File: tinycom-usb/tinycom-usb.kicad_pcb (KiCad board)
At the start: 2 copper layers, 45.2 x 45.2 mm, 65 parts, among them J1 MICRO_SD_HINGE, P1 CONN_02X10, P2 CONN_02X10, P3 USB_A, P4 USB_OTG, U1 SY8008BAAC, U2 AXP209, U3 SY8008BAAC, U4 RTL8188, U5 rainsun-antenna

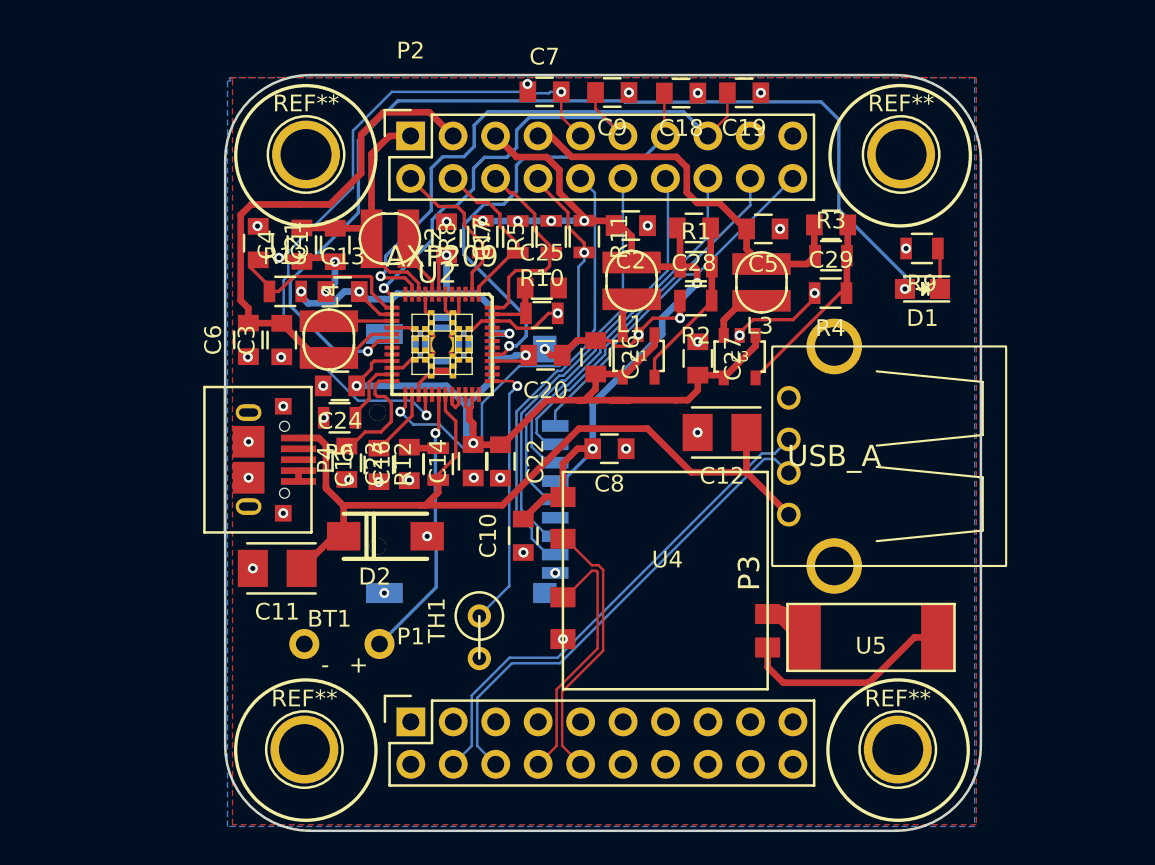
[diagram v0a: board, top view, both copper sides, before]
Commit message: improve tinycom-usb (usb connector+antenna)
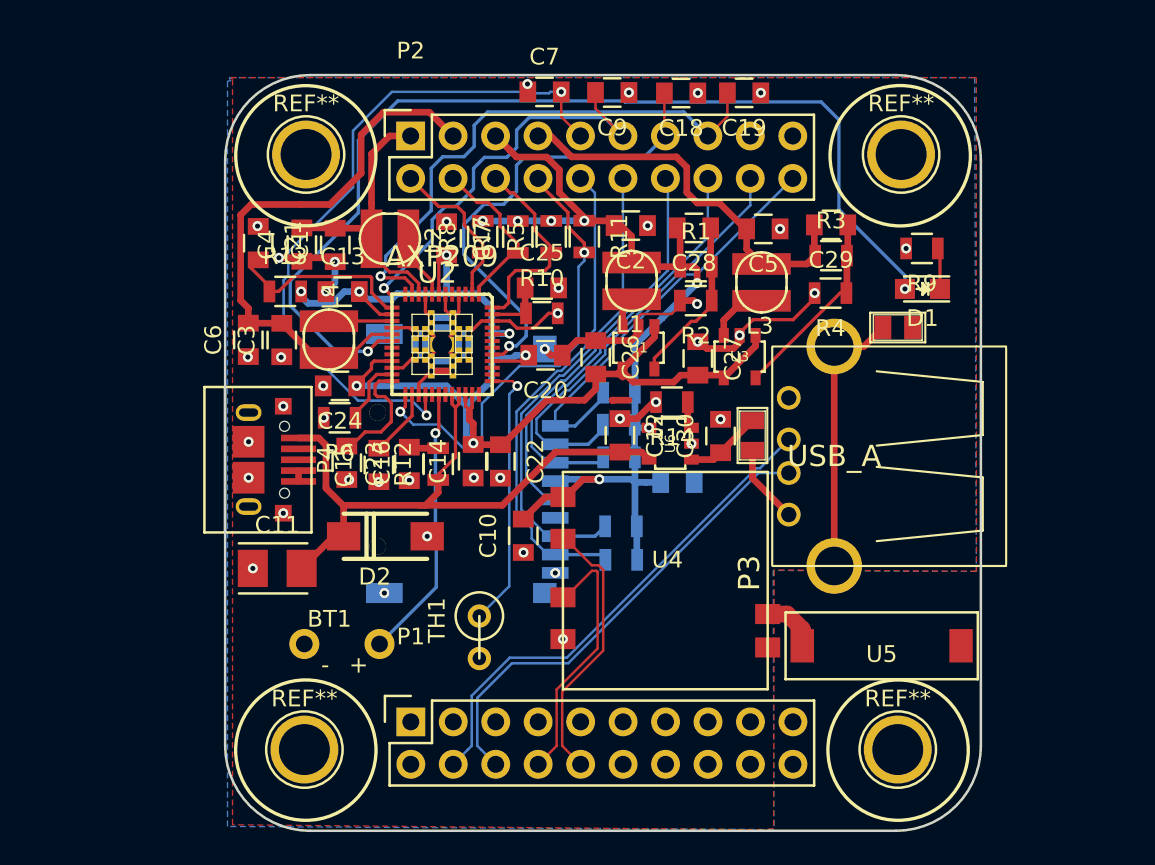
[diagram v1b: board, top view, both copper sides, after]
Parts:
- added C30: 10uF, Capacitors_SMD:C_0805, F.Cu at (154.1, 100.8)
- added L5: SMD-FERRITE-BEAD-200R-2A(0805), OPL-Inductor-L0805, F.Cu at (164.7, 94.4)
- added L6: SMD-FERRITE-BEAD-200R-2A(0805), OPL-Inductor-L0805, F.Cu at (156.0, 100.8)
- added R14: 6.8K, Resistors_SMD:R_0805, F.Cu at (151.2, 98.8)
- added R15: 100K, Resistors_SMD:R_0805, B.Cu at (148.0, 98.3)
- added R16: 100K, Resistors_SMD:R_0805, B.Cu at (148.0, 100.2)
- added R17: 100K, Resistors_SMD:R_0805, B.Cu at (148.0, 102.1)
- added R19: 100K, Resistors_SMD:R_0805, B.Cu at (148.1, 106.2)
- added R20: 100K, Resistors_SMD:R_0805, B.Cu at (148.2, 108.3)
- added U6: SY6280AAC(SOT23-5), opendous:SOT23-5_Opendous, F.Cu at (151.1, 101.3)
- C11: value CP_Small -> 10uF
- C12: value CP_Small -> 10uF; footprint Capacitors_Tantalum_SMD:TantalC_SizeB_EIA-3528_Reflow -> Capacitors_SMD:C_0805
- C8: moved to B.Cu
- U5: footprint tinycom:rainsun-antenna -> tinycom:AN9520
- moved C12 6.11 mm to (148.1, 100.8), turned to 270 degrees
- moved C8 4.54 mm to (151.5, 103.6)
- moved U5 0.81 mm to (163.7, 113.4)
- moved U1 0.49 mm to (149.2, 95.6)
- turned C11 to 0 degrees
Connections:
- C11 pad 1: +5V -> GND
- C11 pad 2: GND -> +5V
- C12 pad 1: +5V -> GND
- C12 pad 2: GND -> +5V
- P3 pad 1: +5V -> USB_5V
- P3 pad 5: GND -> Net-(L5-Pad2)
- U2 pad 31: +5V -> Net-(U2-Pad31)
- U2 pad 32: Net-(U2-Pad32) -> +5V
- U2 pad 33: Net-(U2-Pad32) -> +5V
- U4 pad 5: Net-(U4-Pad5) -> GND
- U5 pad 2: Net-(U4-Pad5) -> Net-(U5-Pad2)
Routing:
- net Net-(L5-Pad2): track 0.00 -> 16.5 mm
- net Net-(U4-Pad5): track 12.9 -> 0.00 mm
- net +5V: track 51.9 -> 39.1 mm
- net VCC_33: track 50.0 -> 58.5 mm, vias 6 -> 7
- net GND: track 63.9 -> 70.5 mm, vias 40 -> 42
- net USB_5V: track 0.00 -> 4.74 mm
- net Net-(C30-Pad1): track 0.00 -> 4.63 mm
- net IPSOUT: track 80.7 -> 76.7 mm
- net SDC0_D2: track 21.1 -> 25.0 mm
- net SDC0_D3: track 22.2 -> 25.7 mm
- net SDC0_D0: track 25.2 -> 28.4 mm
- net SDC0_D1: track 26.2 -> 29.3 mm
- net SDC0_CMD: track 22.4 -> 25.4 mm
- net Net-(U2-Pad32): track 1.71 -> 0.00 mm
- net Net-(R14-Pad1): track 0.00 -> 1.63 mm
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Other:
- net class Default: trace_width 0.4 -> 0.15

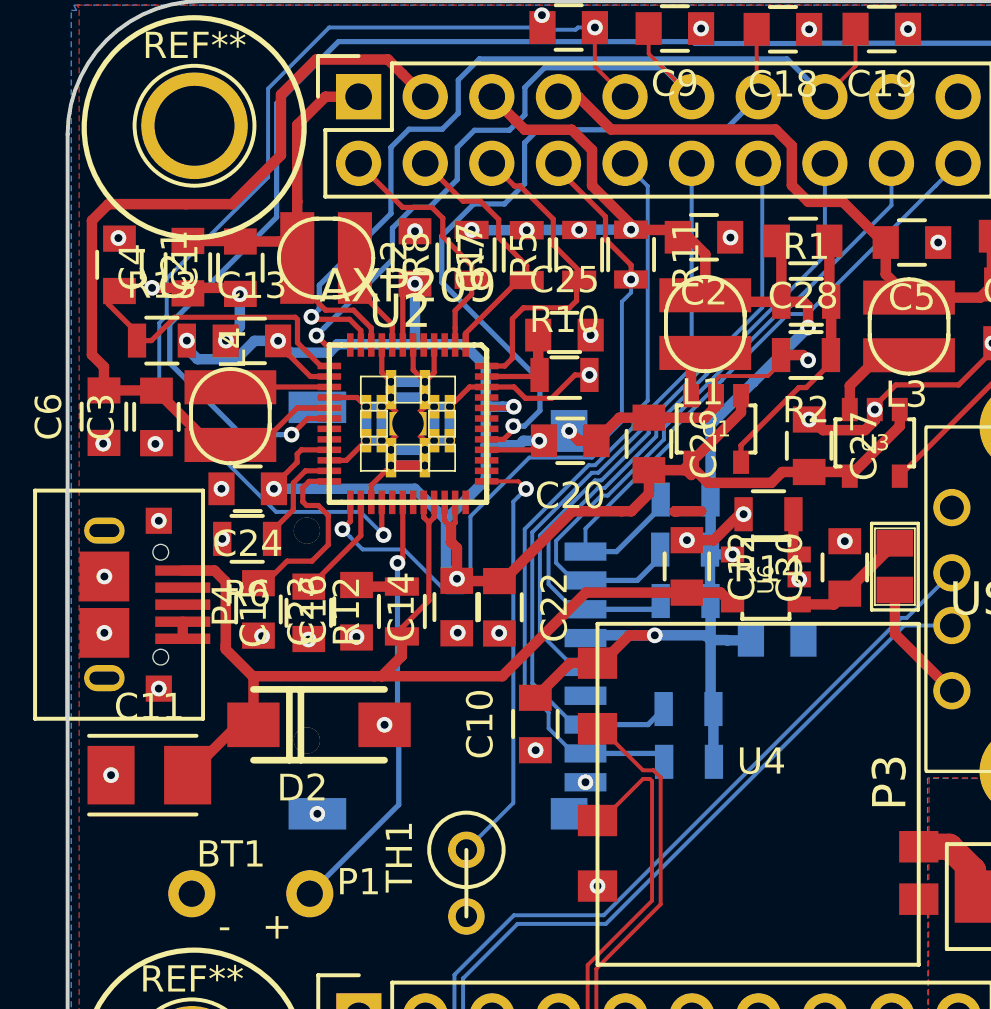
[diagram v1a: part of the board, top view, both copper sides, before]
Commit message: fix tinycom-usb exten
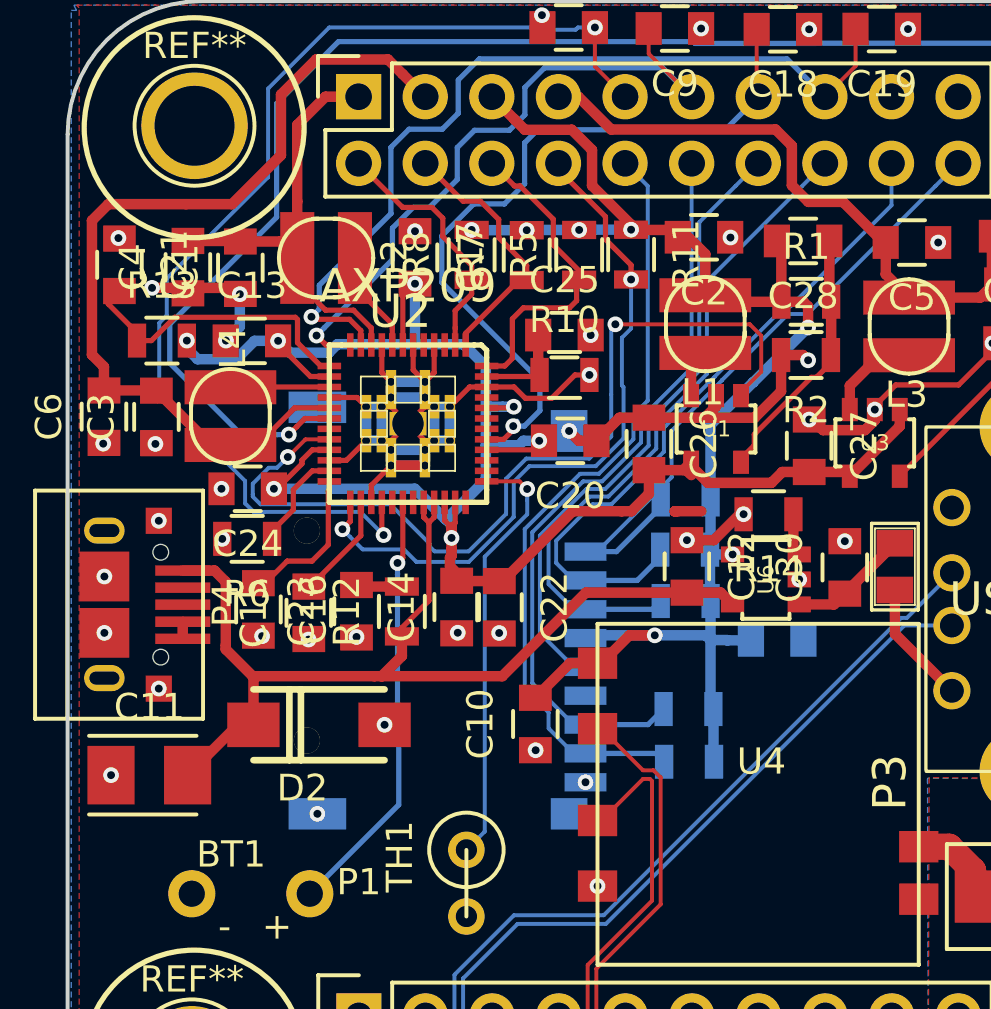
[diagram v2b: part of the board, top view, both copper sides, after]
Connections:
- U1 pad 1: IPSOUT -> EXTEN
- U2 pad 20: Net-(U2-Pad20) -> EXTEN
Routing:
- net EXTEN: track 0.00 -> 34.0 mm, vias 0 -> 2
- net IPSOUT: track 76.7 -> 71.4 mm
- net Net-(C16-Pad1): track 7.12 -> 5.60 mm
- net RESET_N: track 28.3 -> 26.9 mm
- net GND: track 70.5 -> 71.9 mm
- net VCC_13_RTC: track 42.1 -> 42.6 mm
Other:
- net class Default: trace_width 0.15 -> 0.4

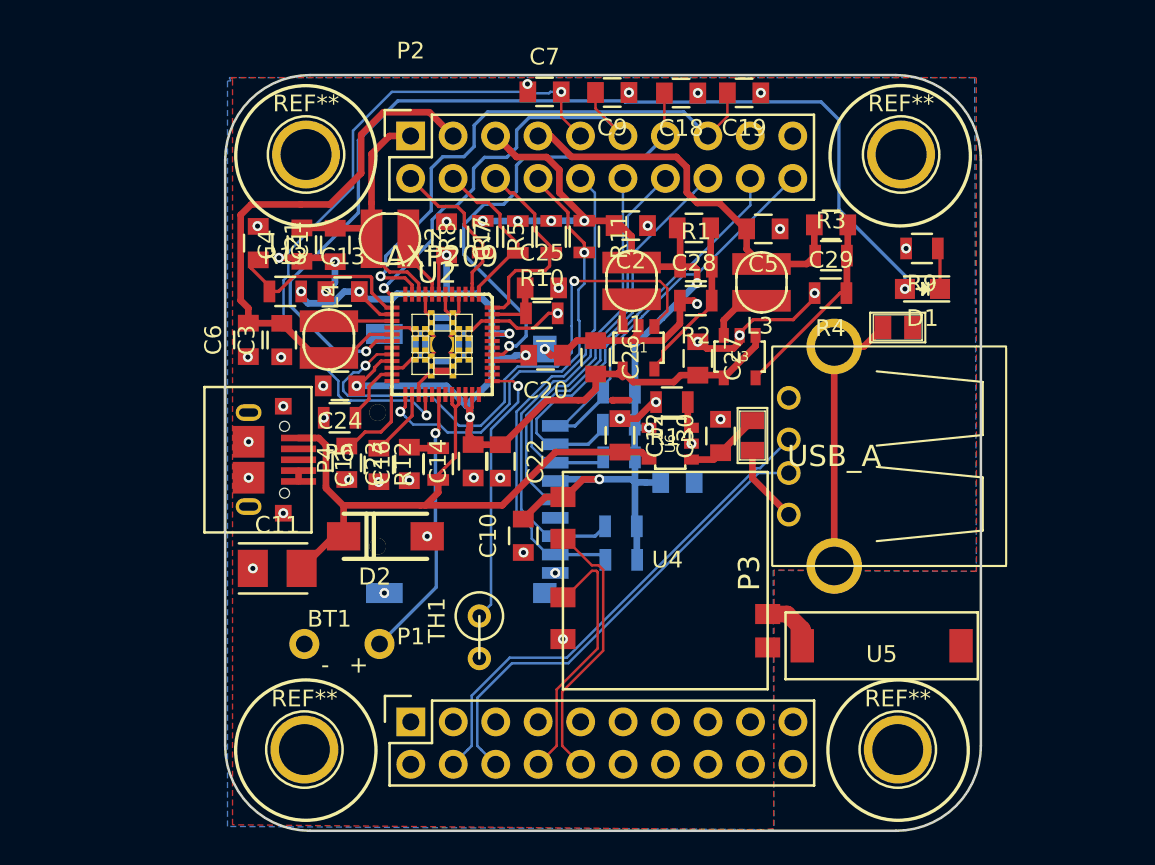
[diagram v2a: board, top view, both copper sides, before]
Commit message: improve tinycom-usb
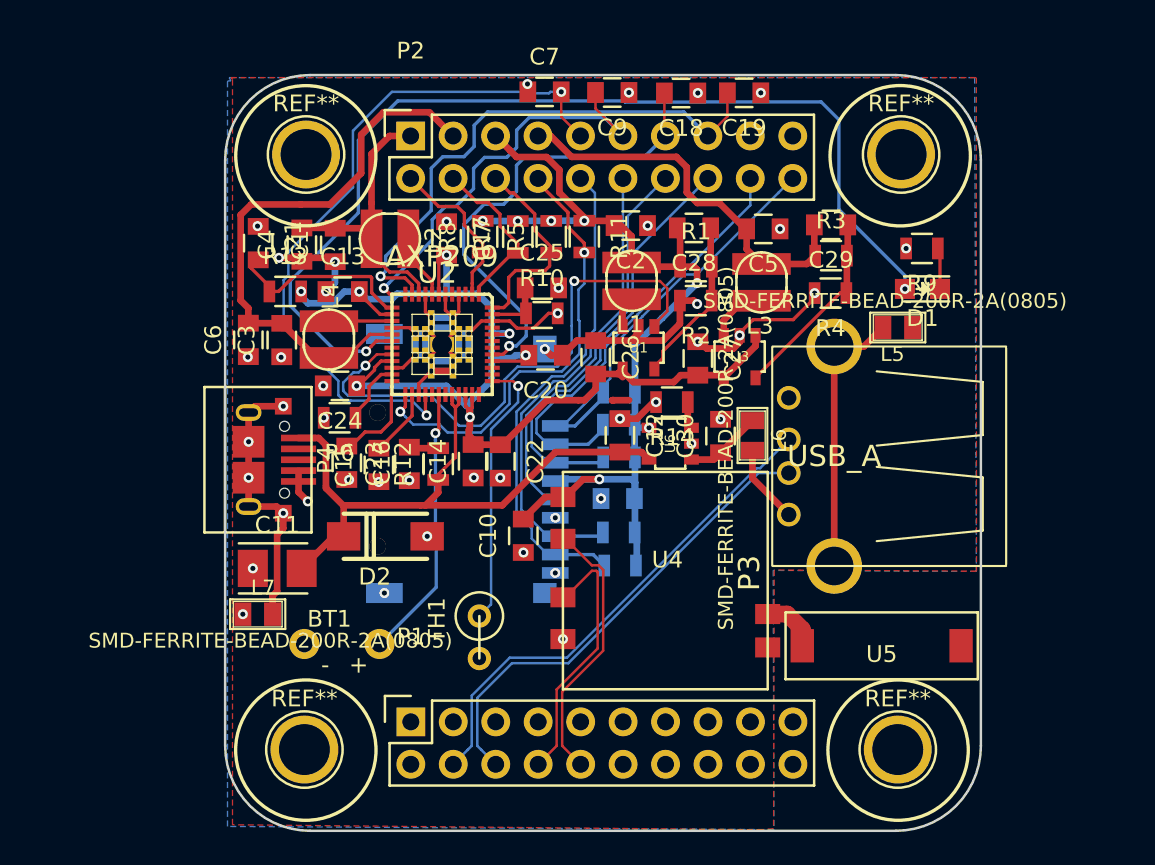
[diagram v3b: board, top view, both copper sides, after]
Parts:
- added L7: SMD-FERRITE-BEAD-200R-2A(0805), OPL-Inductor-L0805, F.Cu at (126.4, 111.5)
- moved C8 3.70 mm to (147.9, 104.6), turned to 0 degrees
- moved G*** 0.89 mm to (155.9, 93.9)
- moved R19 0.39 mm to (148.0, 106.6)
- moved R20 0.35 mm to (148.1, 108.6)
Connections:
- P4 pad 6: GND -> Net-(L7-Pad2)
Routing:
- net Net-(L7-Pad2): track 0.00 -> 16.4 mm, vias 0 -> 4
- net GND: track 71.9 -> 73.3 mm
- net VCC_33: track 58.5 -> 58.0 mm
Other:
- net class Default: trace_width 0.4 -> 0.2

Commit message: improve tinycom-usb
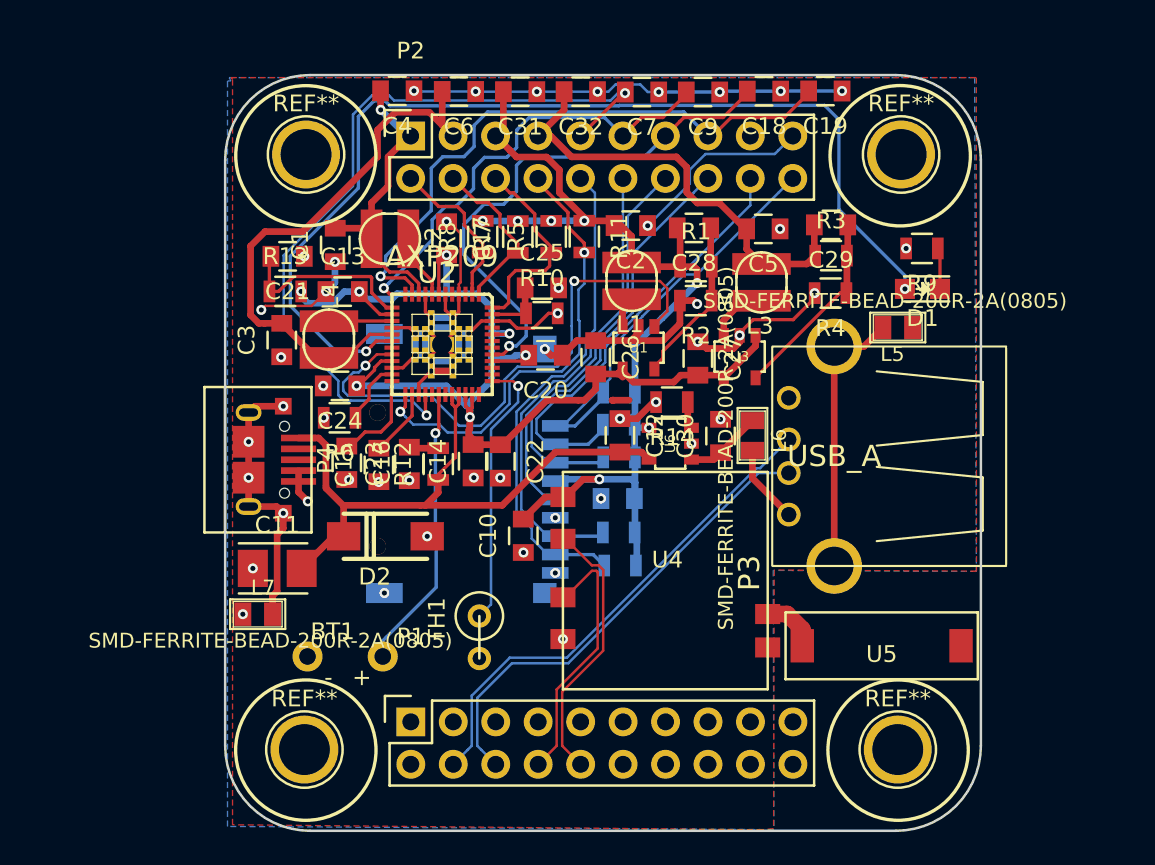
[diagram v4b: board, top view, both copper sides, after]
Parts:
- added C31: 0.1uF, Capacitors_SMD:C_0805, F.Cu at (142.1, 80.2)
- added C32: 0.1uF, Capacitors_SMD:C_0805, F.Cu at (145.7, 80.2)
- moved C6 19.5 mm to (138.4, 80.2), turned to 180 degrees
- moved C4 10.8 mm to (134.8, 80.2), turned to 180 degrees
- moved C7 5.83 mm to (149.4, 80.3), turned to 180 degrees
- moved C9 5.43 mm to (153.0, 80.3)
- moved C18 4.96 mm to (156.7, 80.2)
- moved C19 4.86 mm to (160.4, 80.2)
- moved C21 1.93 mm to (128.2, 90.1), turned to 180 degrees
- moved BT1 0.77 mm to (131.6, 114.0)
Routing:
- net GND: track 73.3 -> 116.2 mm, vias 42 -> 45
- net VCC_13_RTC: track 42.6 -> 48.1 mm
- net LDO4_28: track 32.7 -> 36.9 mm
- net LDO3_28: track 28.8 -> 32.4 mm
- net VCC_15: track 24.1 -> 27.4 mm
- net VCC_33: track 58.0 -> 61.2 mm
- net VCC_30_ANL: track 25.7 -> 27.4 mm
- net VCC_12_CPU: track 17.9 -> 18.9 mm, vias 0 -> 1
- net Net-(D1-Pad2): track 61.0 -> 61.9 mm
- net Net-(BT1-Pad1): track 16.4 -> 17.1 mm
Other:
- net class Default: trace_width 0.2 -> 0.15

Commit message: xxx
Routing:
- net SDC0_D2: track 25.3 -> 22.3 mm
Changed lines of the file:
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@@
   (segment (start 146.18062 101.33838) (end 147.057 100.462) (width 0.2) (layer B.Cu) (net 11))
   (segment (start 147.057 100.462) (end 147.057 100.162) (width 0.2) (layer B.Cu) (net 11))
-  (segment (start 149.417044 93.692956) (end 151.933002 91.176998) (width 0.15) (layer B.Cu) (net 12))
-  (segment (start 152.672002 91.176998) (end 157.553401 86.295599) (width 0.15) (layer B.Cu) (net 12))
+  (segment (start 158.417 85.432) (end 152.672002 91.176998) (width 0.15) (layer B.Cu) (net 12))
+  (segment (start 152.672002 91.176998) (end 151.933002 91.176998) (width 0.15) (layer B.Cu) (net 12))
+  (segment (start 149.417044 93.703504) (end 147.493836 95.62671) (width 0.15) (layer B.Cu) (net 12))
+  (segment (start 151.933002 91.176998) (end 149.417044 93.692956) (width 0.15) (layer B.Cu) (net 12))
+  (segment (start 149.417044 93.692956) (end 149.417044 93.703504) (width 0.15) (layer B.Cu) (net 12))
+  (segment (start 147.493836 95.62671) (end 147.493836 97.886164) (width 0.15) (layer B.Cu) (net 12))
+  (segment (start 147.493836 97.886164) (end 147.128 98.252) (width 0.15) (layer B.Cu) (net 12))
+  (segment (start 147.128 98.252) (end 147.077 98.252) (width 0.15) (layer B.Cu) (net 12))
   (segment (start 144.2085 100.23856) (end 144.65808 100.23856) (width 0.15) (layer B.Cu) (net 12))
-  (segment (start 147.493836 97.402804) (end 147.493836 95.62671) (width 0.15) (layer B.Cu) (net 12))
-  (segment (start 157.553401 86.295599) (end 158.417 85.432) (width 0.15) (layer B.Cu) (net 12))
-  (segment (start 147.493836 95.62671) (end 149.417044 93.703504) (width 0.15) (layer B.Cu) (net 12))
-  (segment (start 144.65808 100.23856) (end 147.493836 97.402804) (width 0.15) (layer B.Cu) (net 12))
-  (segment (start 151.933002 91.176998) (end 152.672002 91.176998) (width 0.15) (layer B.Cu) (net 12))
-  (segment (start 149.417044 93.703504) (end 149.417044 93.692956) (width 0.15) (layer B.Cu) (net 12))
   (segment (start 144.2085 100.23856) (end 145.39044 100.23856) (width 0.2) (layer B.Cu) (net 12))
   (segment (start 145.39044 100.23856) (end 147.077 98.552) (width 0.2) (layer B.Cu) (net 12))
